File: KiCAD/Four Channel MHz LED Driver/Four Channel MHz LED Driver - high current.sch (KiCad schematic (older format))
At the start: 88 parts, among them J10 Conn_01x24_Female, J2 Conn_01x02_Female, J3 8P8C_Shielded_x4, J4 Conn_01x03_Male, J5 Conn_01x03_Female, J6 Conn_01x08_Female, J7 Conn_01x03_Female, J8 Conn_01x05_Female, J9 Conn_01x24_Female, M1 Fan_4pin, Q1 SUM70060E, SW1 Pushbutton_with_LED, SW2 Pushbutton_with_LED, SW3 Pushbutton_with_LED, SW4 Pushbutton_with_LED, SW5 SW_SPDT, U1 12V boost, U12 Teensy3.6, U2 SN74LV4T125PWR, U3 DPBW06F-05, U4 TMUX1204DGSR, U5 BDJ0GA5WEFJ-E2, U6 ADP7182AUJZ-1.8-R7, U7 LT6200CS8-10

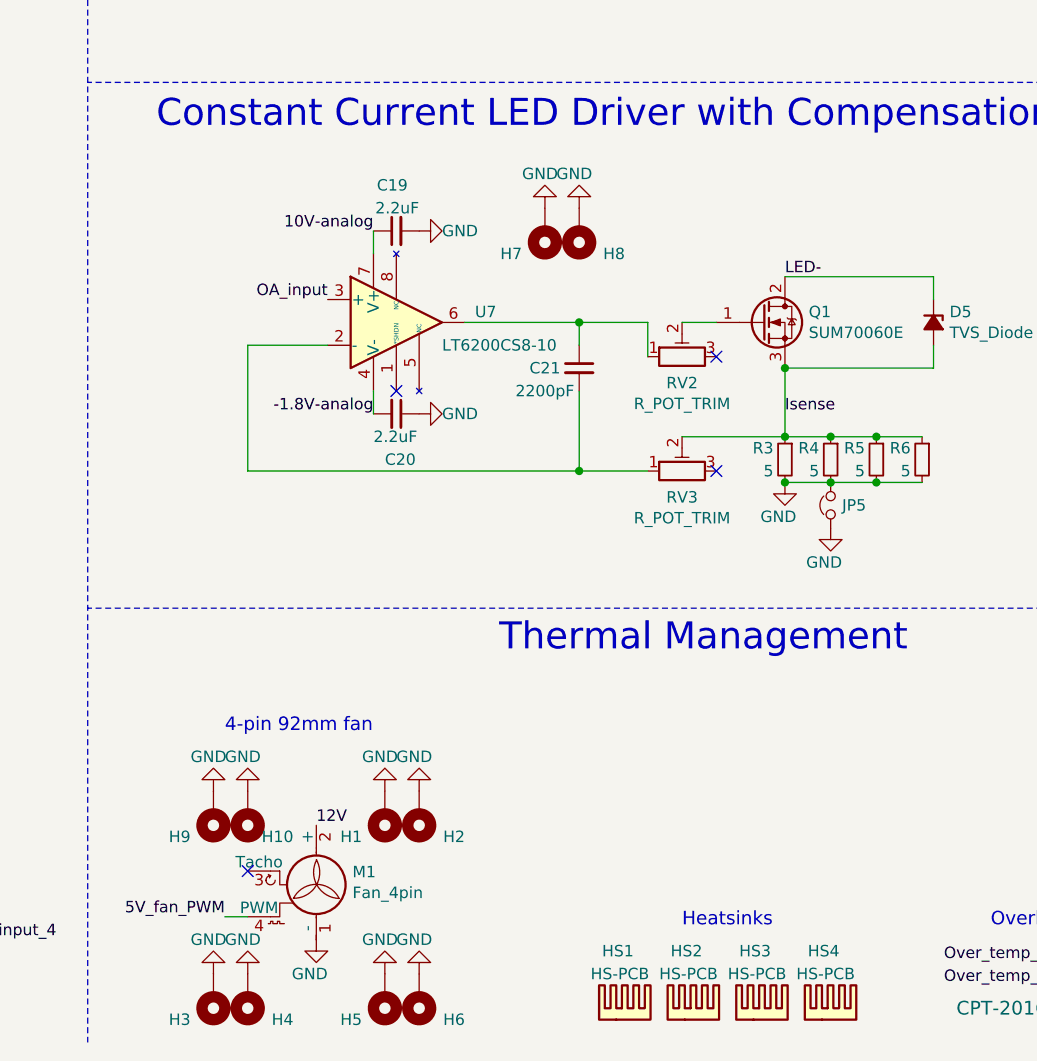
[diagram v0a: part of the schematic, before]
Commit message: Updated layout - still need to update resistors
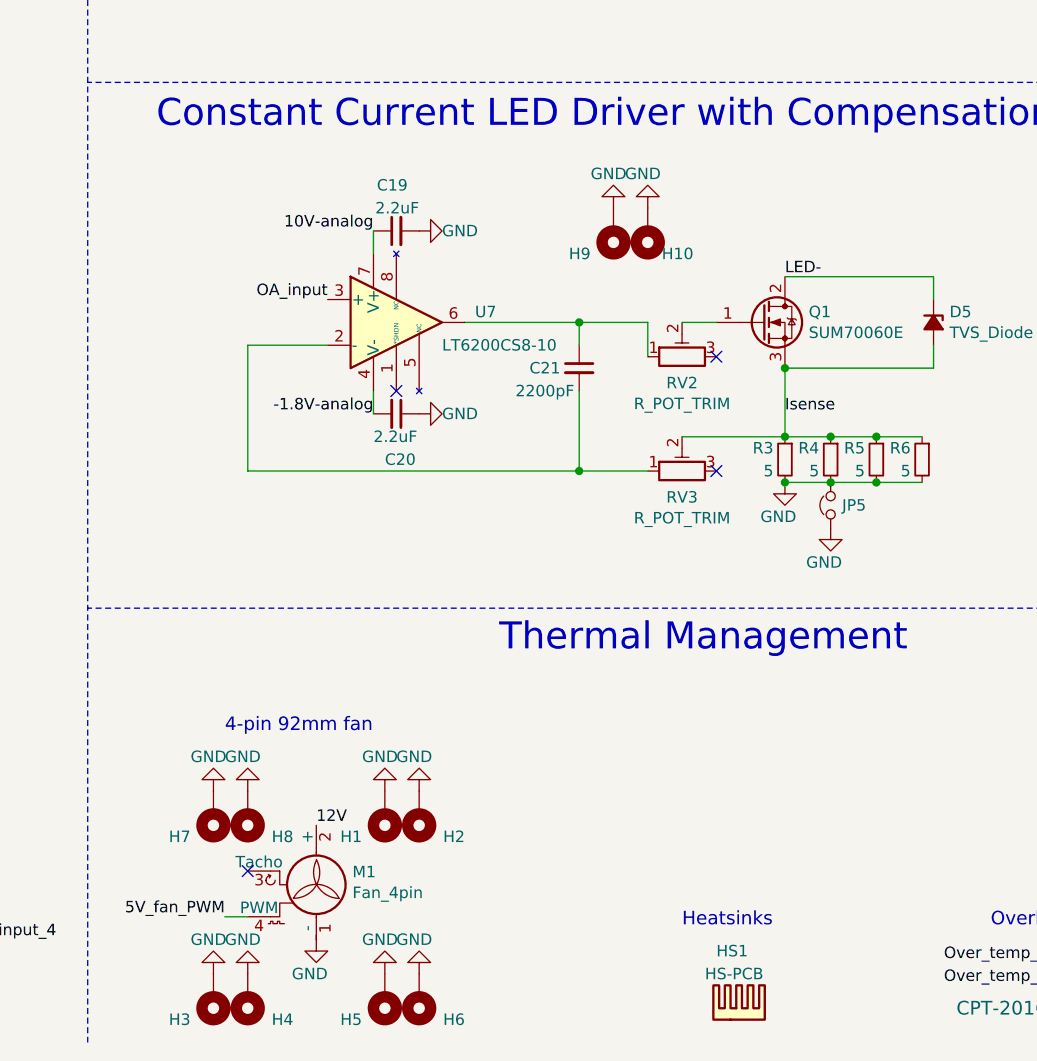
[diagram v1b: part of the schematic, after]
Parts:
- removed HS1, HS2, HS3: HS-PCB, Custom Footprints:Heatsink_910-40-2-23-2-B-0, symbol Mechanical:Heatsink
- H7: footprint Custom Footprints:M2_standoff_ground_via -> Custom Footprints:M4_bolt_hole
- HS1: renamed from HS4; footprint Custom Footprints:Heatsink_910-40-2-23-2-B-0 -> Custom Footprints:Ref_only; Part # 910-40-2-23-2-B-0 -> 125562
- J4: Manufacturer Adam Tech -> Samtec Inc.; Part # PH1RB-03-UA -> TSM-103-01-L-SV
- J5: Manufacturer Samtec Inc. -> (none); Part # SSM-103-L-SV -> (none)
- JP1: footprint Custom Footprints:4928TR-LED -> Custom Footprints:4928TR-power
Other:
- moved on the sheet: H10, H7, H8, H9, HS1

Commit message: update
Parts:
- R3, R4, R5, R6: value 5 -> 0.2; footprint Custom Footprints:TO-252_resistor -> Custom Footprints:Rideon_PFS35_resistor; Manufacturer Ohmite -> Riedon; Part # TKH45P5R00FE-TR -> PFS35-0R2F1
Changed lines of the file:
@@
 	1    0    0    -1
-$EndComp
-$Comp
-L Device:R_Small R5
-U 1 1 5F599BF8
-P 10150 8650
-F 0 "R5" H 10200 8700 50  0000 L CNN
-F 1 "5" H 10200 8600 50  0000 L CNN
-F 2 "Custom Footprints:TO-252_resistor" H 10150 8650 50  0001 C CNN
-F 3 "http://www.ohmite.com/assets/docs/res_tkh.pdf?r=false" H 10150 8650 50  0001 C CNN
-F 4 "Ohmite" H 10150 8650 50  0001 C CNN "Manufacturer"
-F 5 "TKH45P5R00FE-TR" H 10150 8650 50  0001 C CNN "Part #"
-	1    10150 8650
-	-1   0    0    -1
 $EndComp
 Text Notes 5200 3100 0    50   ~ 0
@@
 	9750 8250 9750 8550
 $Comp
-L Device:R_Small R6
-U 1 1 5F57BF27
-P 10350 8650
-F 0 "R6" H 10400 8700 50  0000 L CNN
-F 1 "5" H 10400 8600 50  0000 L CNN
-F 2 "Custom Footprints:TO-252_resistor" H 10350 8650 50  0001 C CNN
-F 3 "http://www.ohmite.com/assets/docs/res_tkh.pdf?r=false" H 10350 8650 50  0001 C CNN
-F 4 "Ohmite" H 10350 8650 50  0001 C CNN "Manufacturer"
-F 5 "TKH45P5R00FE-TR" H 10350 8650 50  0001 C CNN "Part #"
-	1    10350 8650
-	-1   0    0    -1
-$EndComp
-$Comp
 L Device:R_Small R3
 U 1 1 5F57C598
 P 9750 8650
 F 0 "R3" H 9800 8700 50  0000 L CNN
-F 1 "5" H 9800 8600 50  0000 L CNN
-F 2 "Custom Footprints:TO-252_resistor" H 9750 8650 50  0001 C CNN
-F 3 "http://www.ohmite.com/assets/docs/res_tkh.pdf?r=false" H 9750 8650 50  0001 C CNN
-F 4 "Ohmite" H 9750 8650 50  0001 C CNN "Manufacturer"
-F 5 "TKH45P5R00FE-TR" H 9750 8650 50  0001 C CNN "Part #"
+F 1 "0.2" H 9800 8600 50  0000 L CNN
+F 2 "Custom Footprints:Rideon_PFS35_resistor" H 9750 8650 50  0001 C CNN
+F 3 "https://riedon.com/media/pdf/PFS35.pdf" H 9750 8650 50  0001 C CNN
+F 4 "Riedon" H 9750 8650 50  0001 C CNN "Manufacturer"
+F 5 "PFS35-0R2F1" H 9750 8650 50  0001 C CNN "Part #"
 	1    9750 8650
-	-1   0    0    -1
-$EndComp
-$Comp
-L Device:R_Small R4
-U 1 1 5F57CB17
-P 9950 8650
-F 0 "R4" H 10000 8700 50  0000 L CNN
-F 1 "5" H 10000 8600 50  0000 L CNN
-F 2 "Custom Footprints:TO-252_resistor" H 9950 8650 50  0001 C CNN
-F 3 "http://www.ohmite.com/assets/docs/res_tkh.pdf?r=false" H 9950 8650 50  0001 C CNN
-F 4 "Ohmite" H 9950 8650 50  0001 C CNN "Manufacturer"
-F 5 "TKH45P5R00FE-TR" H 9950 8650 50  0001 C CNN "Part #"
-	1    9950 8650
 	-1   0    0    -1
 $EndComp
@@
 Connection ~ 9750 8750
 Wire Wire Line
-	9750 8550 9950 8550
-Wire Wire Line
 	9750 8750 9950 8750
-Connection ~ 9950 8550
 Connection ~ 9950 8750
-Wire Wire Line
-	9950 8550 10150 8550
-Wire Wire Line
-	9950 8750 10150 8750
-Connection ~ 10150 8550
-Wire Wire Line
-	10150 8550 10350 8550
-Connection ~ 10150 8750
-Wire Wire Line
-	10150 8750 10350 8750
 $Comp
 L Device:R_Small R2
@@
 	-1   0    0    1
 $EndComp
+Wire Wire Line
+	9750 8550 9950 8550
+Wire Wire Line
+	9950 8750 10150 8750
+$Comp
+L Device:R_Small R4
+U 1 1 60D436CE
+P 9950 8650
+F 0 "R4" H 10000 8700 50  0000 L CNN
+F 1 "0.2" H 10000 8600 50  0000 L CNN
+F 2 "Custom Footprints:Rideon_PFS35_resistor" H 9950 8650 50  0001 C CNN
+F 3 "https://riedon.com/media/pdf/PFS35.pdf" H 9950 8650 50  0001 C CNN
+F 4 "Riedon" H 9950 8650 50  0001 C CNN "Manufacturer"
+F 5 "PFS35-0R2F1" H 9950 8650 50  0001 C CNN "Part #"
+	1    9950 8650
+	-1   0    0    -1
+$EndComp
+Connection ~ 9950 8550
+Wire Wire Line
+	9950 8550 10150 8550
+$Comp
+L Device:R_Small R5
+U 1 1 60D43C91
+P 10150 8650
+F 0 "R5" H 10200 8700 50  0000 L CNN
+F 1 "0.2" H 10200 8600 50  0000 L CNN
+F 2 "Custom Footprints:Rideon_PFS35_resistor" H 10150 8650 50  0001 C CNN
+F 3 "https://riedon.com/media/pdf/PFS35.pdf" H 10150 8650 50  0001 C CNN
+F 4 "Riedon" H 10150 8650 50  0001 C CNN "Manufacturer"
+F 5 "PFS35-0R2F1" H 10150 8650 50  0001 C CNN "Part #"
+	1    10150 8650
+	-1   0    0    -1
+$EndComp
+Connection ~ 10150 8550
+Wire Wire Line
+	10150 8550 10350 8550
+Connection ~ 10150 8750
+Wire Wire Line
+	10150 8750 10350 8750
+$Comp
+L Device:R_Small R6
+U 1 1 60D44267
+P 10350 8650
+F 0 "R6" H 10400 8700 50  0000 L CNN
+F 1 "0.2" H 10400 8600 50  0000 L CNN
+F 2 "Custom Footprints:Rideon_PFS35_resistor" H 10350 8650 50  0001 C CNN
+F 3 "https://riedon.com/media/pdf/PFS35.pdf" H 10350 8650 50  0001 C CNN
+F 4 "Riedon" H 10350 8650 50  0001 C CNN "Manufacturer"
+F 5 "PFS35-0R2F1" H 10350 8650 50  0001 C CNN "Part #"
+	1    10350 8650
+	-1   0    0    -1
+$EndComp
 $EndSCHEMATC

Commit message: Driver updates
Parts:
- RN3: footprint Custom Footprints:2506_modified_concave_8x_R-pack -> Custom Footprints:1506-EXB-2HV472JV-for_2_oz_pour; Manufacturer CTS Resistor Products -> Panasonic Electronic Components; Part # 742C163472JP -> EXB-2HV472JV
- RN3: footprint Custom Footprints:2506_modified_concave_8x_R-pack -> Custom Footprints:1506-EXB-2HV472JV-for_2_oz_pour
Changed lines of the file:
@@
 F 0 "RN3" V 4700 7650 50  0000 C CNN
 F 1 "4.7k" V 4600 7650 50  0000 C CNN
-F 2 "Custom Footprints:2506_modified_concave_8x_R-pack" V 5075 7650 50  0001 C CNN
-F 3 "https://www.ctscorp.com/wp-content/uploads/74x.pdf" H 4600 7650 50  0001 C CNN
+F 2 "Custom Footprints:1506-EXB-2HV472JV-for_2_oz_pour" V 5075 7650 50  0001 C CNN
+F 3 "https://industrial.panasonic.com/cdbs/www-data/pdf/AOC0000/AOC0000C14.pdf" H 4600 7650 50  0001 C CNN
 F 4 "CTS Resistor Products" V 4600 7650 50  0001 C CNN "Manufacturer"
 F 5 "742C163472JP" V 4600 7650 50  0001 C CNN "Part #"
@@
 F 0 "RN3" V 4500 7500 50  0000 C CNN
 F 1 "4.7k" V 4600 7500 50  0000 C CNN
-F 2 "Custom Footprints:2506_modified_concave_8x_R-pack" V 5075 7500 50  0001 C CNN
-F 3 "https://www.ctscorp.com/wp-content/uploads/74x.pdf" H 4600 7500 50  0001 C CNN
+F 2 "Custom Footprints:1506-EXB-2HV472JV-for_2_oz_pour" V 5075 7500 50  0001 C CNN
+F 3 "https://industrial.panasonic.com/cdbs/www-data/pdf/AOC0000/AOC0000C14.pdf" H 4600 7500 50  0001 C CNN
 F 4 "CTS Resistor Products" V 4600 7500 50  0001 C CNN "Manufacturer"
 F 5 "742C163472JP" V 4600 7500 50  0001 C CNN "Part #"
@@
 F 0 "RN3" V 1900 7950 50  0000 C CNN
 F 1 "4.7k" V 2000 7950 50  0000 C CNN
-F 2 "Custom Footprints:2506_modified_concave_8x_R-pack" V 2475 7950 50  0001 C CNN
-F 3 "https://www.ctscorp.com/wp-content/uploads/74x.pdf" H 2000 7950 50  0001 C CNN
+F 2 "Custom Footprints:1506-EXB-2HV472JV-for_2_oz_pour" V 2475 7950 50  0001 C CNN
+F 3 "https://industrial.panasonic.com/cdbs/www-data/pdf/AOC0000/AOC0000C14.pdf" H 2000 7950 50  0001 C CNN
 F 4 "CTS Resistor Products" V 2000 7950 50  0001 C CNN "Manufacturer"
 F 5 "742C163472JP" V 2000 7950 50  0001 C CNN "Part #"
@@
 F 0 "RN3" V 1900 8150 50  0000 C CNN
 F 1 "4.7k" V 2000 8150 50  0000 C CNN
-F 2 "Custom Footprints:2506_modified_concave_8x_R-pack" V 2475 8150 50  0001 C CNN
-F 3 "https://www.ctscorp.com/wp-content/uploads/74x.pdf" H 2000 8150 50  0001 C CNN
+F 2 "Custom Footprints:1506-EXB-2HV472JV-for_2_oz_pour" V 2475 8150 50  0001 C CNN
+F 3 "https://industrial.panasonic.com/cdbs/www-data/pdf/AOC0000/AOC0000C14.pdf" H 2000 8150 50  0001 C CNN
 F 4 "CTS Resistor Products" V 2000 8150 50  0001 C CNN "Manufacturer"
 F 5 "742C163472JP" V 2000 8150 50  0001 C CNN "Part #"
@@
 F 0 "RN3" V 4700 7850 50  0000 C CNN
 F 1 "4.7k" V 4600 7850 50  0000 C CNN
-F 2 "Custom Footprints:2506_modified_concave_8x_R-pack" V 5075 7850 50  0001 C CNN
-F 3 "https://www.ctscorp.com/wp-content/uploads/74x.pdf" H 4600 7850 50  0001 C CNN
+F 2 "Custom Footprints:1506-EXB-2HV472JV-for_2_oz_pour" V 5075 7850 50  0001 C CNN
+F 3 "https://industrial.panasonic.com/cdbs/www-data/pdf/AOC0000/AOC0000C14.pdf" H 4600 7850 50  0001 C CNN
 F 4 "CTS Resistor Products" V 4600 7850 50  0001 C CNN "Manufacturer"
 F 5 "742C163472JP" V 4600 7850 50  0001 C CNN "Part #"
@@
 F 0 "RN3" V 1900 8350 50  0000 C CNN
 F 1 "4.7k" V 2000 8350 50  0000 C CNN
-F 2 "Custom Footprints:2506_modified_concave_8x_R-pack" V 2475 8350 50  0001 C CNN
-F 3 "https://www.ctscorp.com/wp-content/uploads/74x.pdf" H 2000 8350 50  0001 C CNN
-F 4 "CTS Resistor Products" V 2000 8350 50  0001 C CNN "Manufacturer"
-F 5 "742C163472JP" V 2000 8350 50  0001 C CNN "Part #"
+F 2 "Custom Footprints:1506-EXB-2HV472JV-for_2_oz_pour" V 2475 8350 50  0001 C CNN
+F 3 "https://industrial.panasonic.com/cdbs/www-data/pdf/AOC0000/AOC0000C14.pdf" H 2000 8350 50  0001 C CNN
+F 4 "Panasonic Electronic Components" V 2000 8350 50  0001 C CNN "Manufacturer"
+F 5 "EXB-2HV472JV" V 2000 8350 50  0001 C CNN "Part #"
 	1    2000 8350
 	0    1    -1   0
@@
 F 0 "RN3" V 2850 9200 50  0000 C CNN
 F 1 "4.7k" V 2750 9200 50  0000 C CNN
-F 2 "Custom Footprints:2506_modified_concave_8x_R-pack" V 3225 9200 50  0001 C CNN
-F 3 "https://www.ctscorp.com/wp-content/uploads/74x.pdf" H 2750 9200 50  0001 C CNN
+F 2 "Custom Footprints:1506-EXB-2HV472JV-for_2_oz_pour" V 3225 9200 50  0001 C CNN
+F 3 "https://industrial.panasonic.com/cdbs/www-data/pdf/AOC0000/AOC0000C14.pdf" H 2750 9200 50  0001 C CNN
 F 4 "CTS Resistor Products" V 2750 9200 50  0001 C CNN "Manufacturer"
 F 5 "742C163472JP" V 2750 9200 50  0001 C CNN "Part #"
@@
 F 0 "RN3" V 1900 7750 50  0000 C CNN
 F 1 "4.7k" V 2000 7750 50  0000 C CNN
-F 2 "Custom Footprints:2506_modified_concave_8x_R-pack" V 2475 7750 50  0001 C CNN
-F 3 "https://www.ctscorp.com/wp-content/uploads/74x.pdf" H 2000 7750 50  0001 C CNN
+F 2 "Custom Footprints:1506-EXB-2HV472JV-for_2_oz_pour" V 2475 7750 50  0001 C CNN
+F 3 "https://industrial.panasonic.com/cdbs/www-data/pdf/AOC0000/AOC0000C14.pdf" H 2000 7750 50  0001 C CNN
 F 4 "CTS Resistor Products" V 2000 7750 50  0001 C CNN "Manufacturer"
 F 5 "742C163472JP" V 2000 7750 50  0001 C CNN "Part #"
